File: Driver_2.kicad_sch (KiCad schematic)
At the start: 34 parts

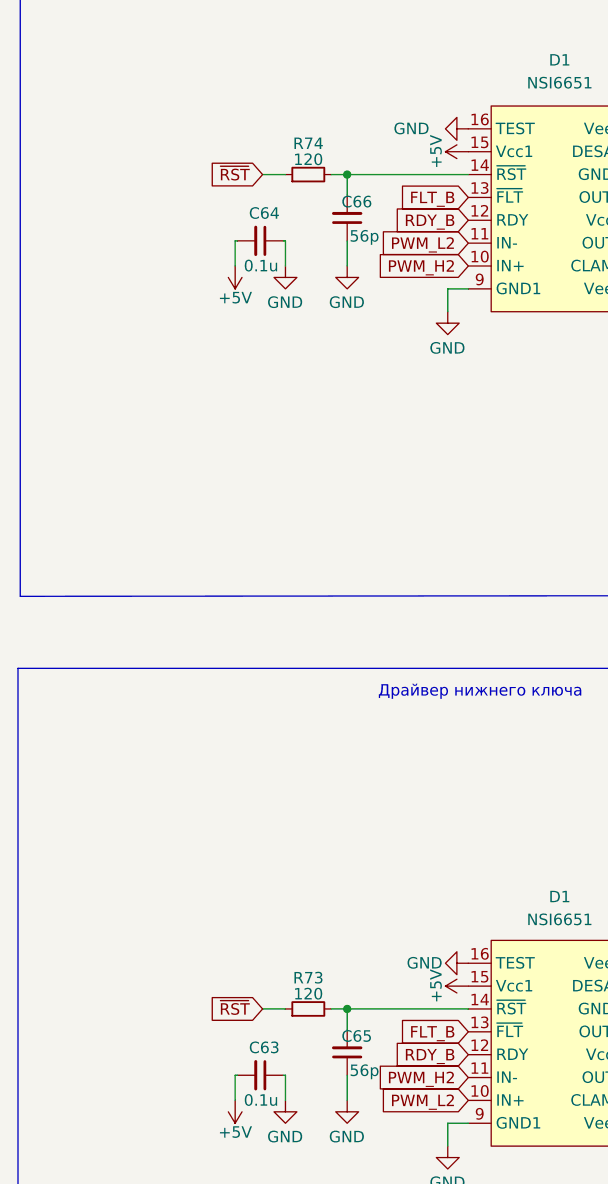
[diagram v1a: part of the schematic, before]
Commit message: Отправил на проверку в резонит: изменил BOM
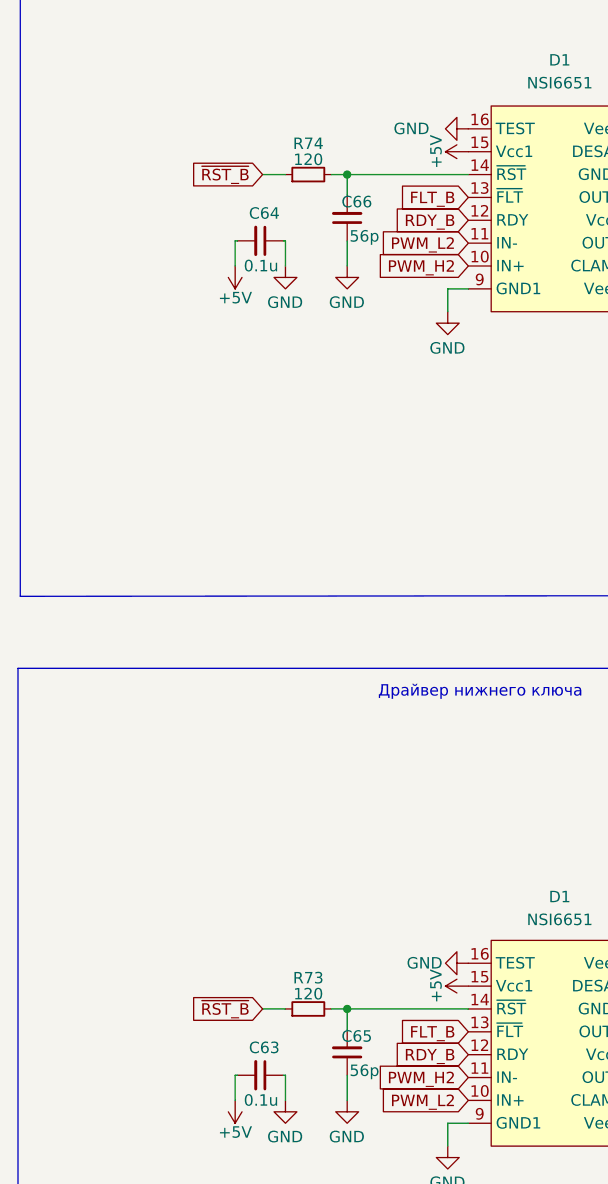
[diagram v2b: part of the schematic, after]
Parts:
- D41, D42, D60, D62: value MURS360T3G -> MURS160
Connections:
- net ~{RST} renamed ~{RST_B}
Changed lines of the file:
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@@
+		)
+	)
+	(global_label "~{RST_B}"
+		(shape input)
+		(at 58.42 146.05 180)
+		(fields_autoplaced yes)
+		(effects
+			(font
+				(size 1.27 1.27)
+			)
+			(justify right)
+		)
+		(property "Intersheetrefs" "${INTERSHEET_REFS}"
+			(at 49.7501 146.05 0)
+			(effects
+				(font
+					(size 1.27 1.27)
+				)
+				(justify right)
+				(hide yes)
+			)
 		)
 	)
@@
 		)
 	)
+	(global_label "~{RST_B}"
+		(shape input)
+		(at 58.42 53.34 180)
+		(fields_autoplaced yes)
+		(effects
+			(font
+				(size 1.27 1.27)
+			)
+			(justify right)
+		)
+		(property "Intersheetrefs" "${INTERSHEET_REFS}"
+			(at 49.7501 53.34 0)
+			(effects
+				(font
+					(size 1.27 1.27)
+				)
+				(justify right)
+				(hide yes)
+			)
+		)
+	)
 	(global_label "+15V_L2"
 		(shape input)
@@
 		)
 	)
-	(global_label "~{RST}"
-		(shape input)
-		(at 58.42 146.05 180)
-		(fields_autoplaced yes)
-		(effects
-			(font
-				(size 1.27 1.27)
-			)
-			(justify right)
-		)
-		(property "Intersheetrefs" "${INTERSHEET_REFS}"
-			(at 52.605 146.05 0)
-			(effects
-				(font
-					(size 1.27 1.27)
-				)
-				(justify right)
-				(hide yes)
-			)
-		)
-	)
 	(global_label "C3"
 		(shape input)
@@
 		)
 	)
-	(global_label "~{RST}"
-		(shape input)
-		(at 58.42 53.34 180)
-		(fields_autoplaced yes)
-		(effects
-			(font
-				(size 1.27 1.27)
-			)
-			(justify right)
-		)
-		(property "Intersheetrefs" "${INTERSHEET_REFS}"
-			(at 52.605 53.34 0)
-			(effects
-				(font
-					(size 1.27 1.27)
-				)
-				(justify right)
-				(hide yes)
-			)
-		)
-	)
 	(global_label "-15V_H2"
 		(shape input)
@@
 			)
 		)
-		(property "Value" "MURS360T3G"
+		(property "Value" "MURS160"
 			(at 131.318 68.834 0)
 			(effects
@@
 			)
 		)
-		(property "Value" "MURS360T3G"
+		(property "Value" "MURS160"
 			(at 153.924 146.05 0)
 			(effects
@@
 			)
 		)
-		(property "Value" "MURS360T3G"
+		(property "Value" "MURS160"
 			(at 131.318 73.914 0)
 			(effects
@@
 			)
 		)
-		(property "Value" "MURS360T3G"
+		(property "Value" "MURS160"
 			(at 148.844 146.05 0)
 			(effects

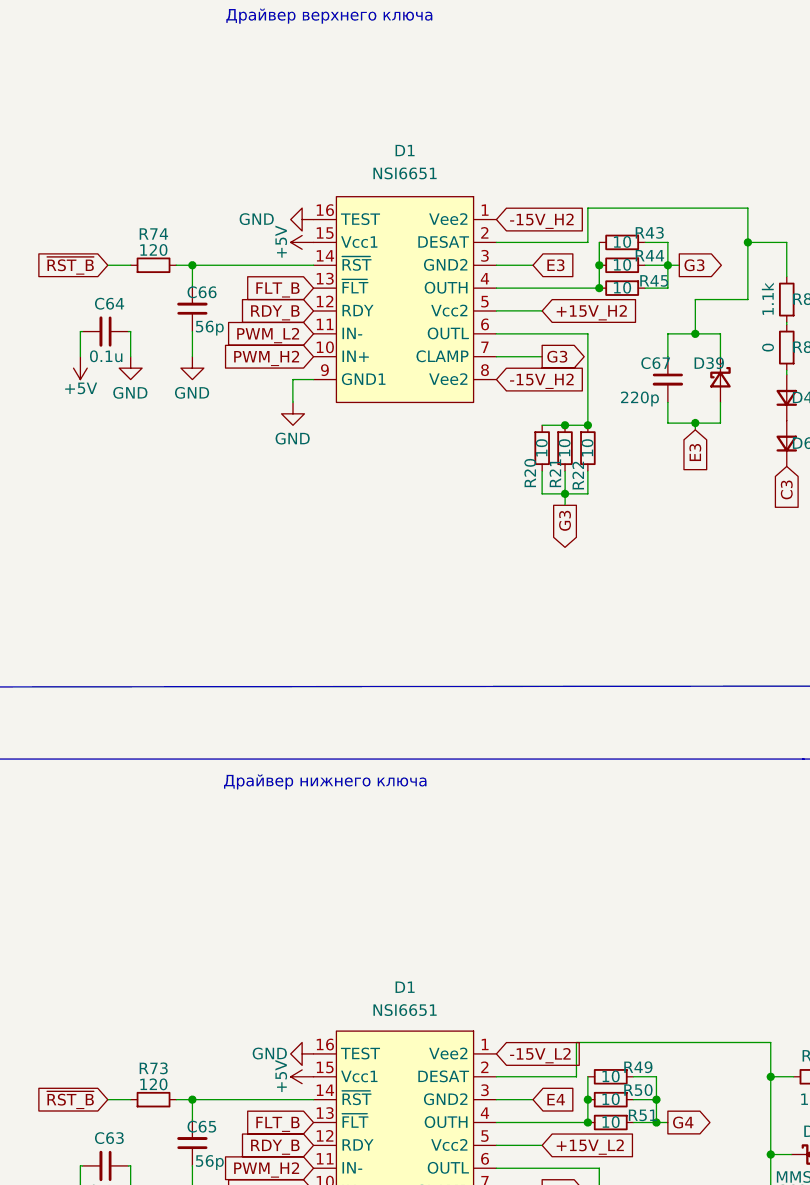
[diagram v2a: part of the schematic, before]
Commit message: Изменения: обновил BOM и названия в схеме
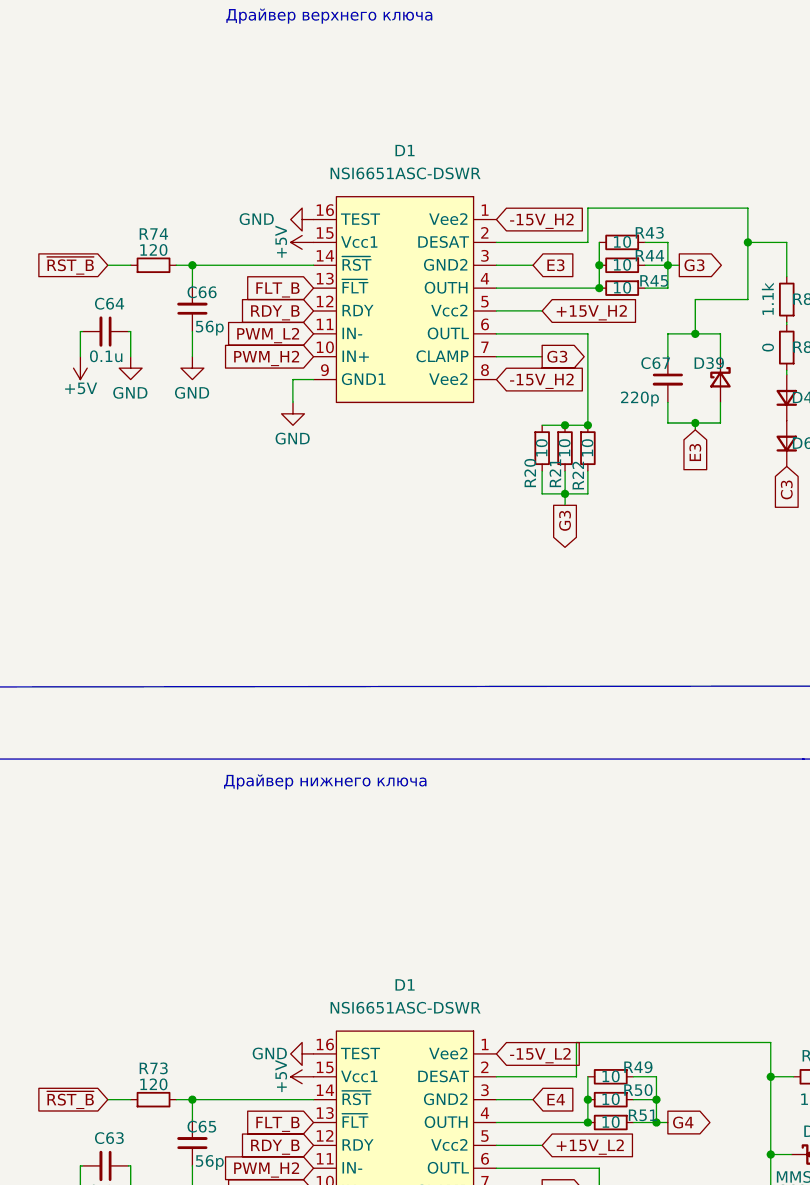
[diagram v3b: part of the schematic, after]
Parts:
- D1: value NSI6651 -> NSI6651ASC-DSWR
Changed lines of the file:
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@@
 			)
 		)
-		(property "Value" "NSI6651"
+		(property "Value" "NSI6651ASC-DSWR"
 			(at 91.44 43.18 0)
 			(effects
@@
 		(fields_autoplaced yes)
 		(property "Reference" "D1"
-			(at 91.44 133.604 0)
-			(effects
-				(font
-					(size 1.27 1.27)
-				)
-			)
-		)
-		(property "Value" "NSI6651"
-			(at 91.44 136.144 0)
-			(effects
-				(font
+			(at 91.44 133.35 0)
+			(effects
+				(font
+					(size 1.27 1.27)
+				)
+			)
+		)
+		(property "Value" "NSI6651ASC-DSWR"
+			(at 91.44 135.89 0)
+			(effects
+				(font

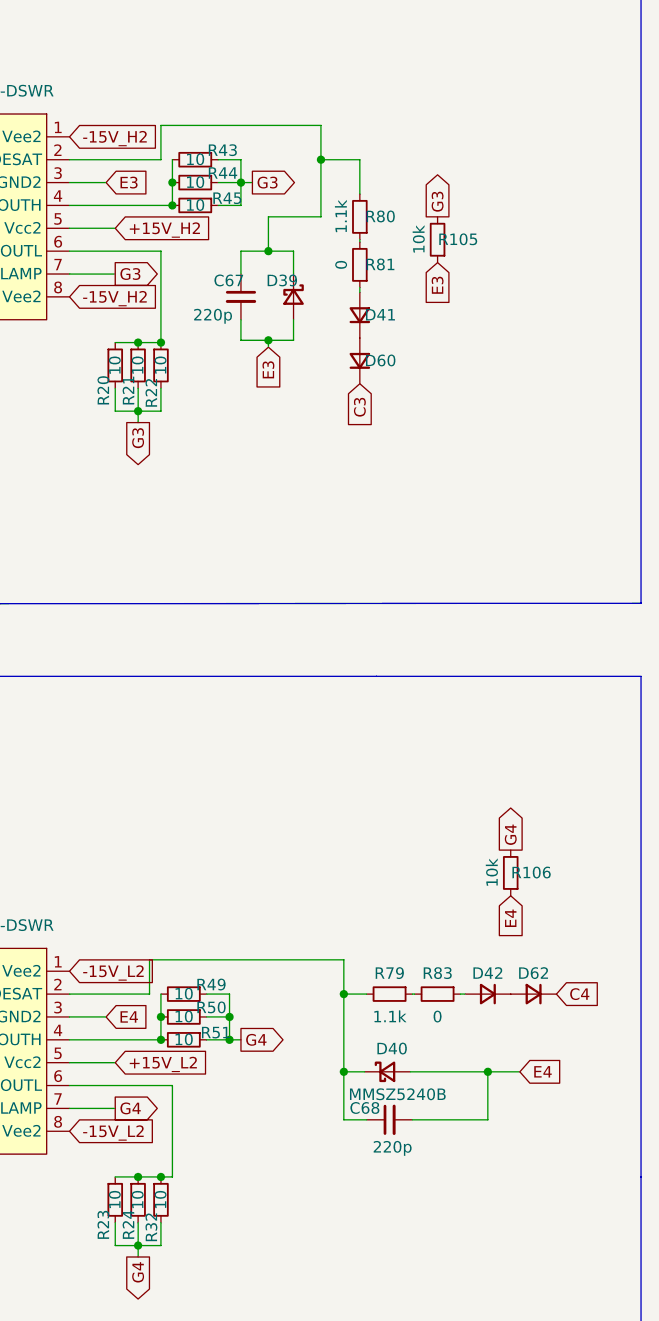
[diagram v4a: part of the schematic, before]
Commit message: Изменения: поменял трассировку полигонов, изменил трассировку цепи DESAT в фазе А
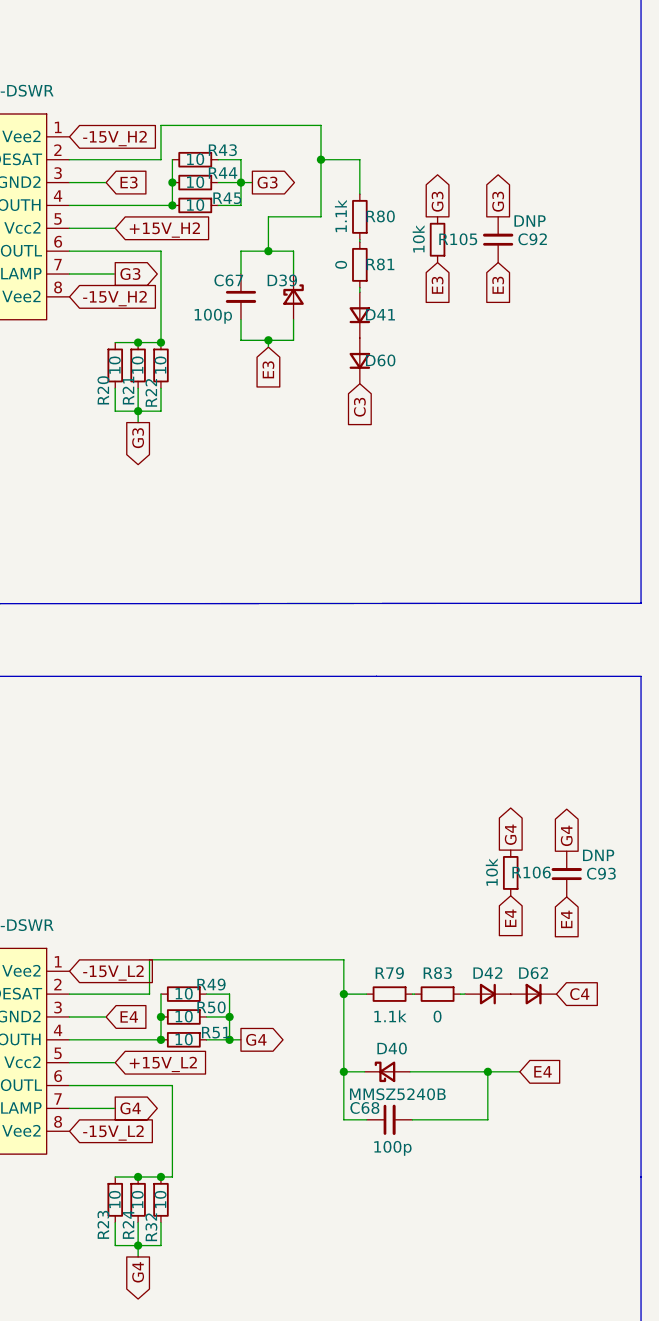
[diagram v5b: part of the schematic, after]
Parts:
- added C92, C93: DNP, Capacitor_SMD:C_0805_2012Metric_Pad1.18x1.45mm_HandSolder, symbol Device:C_Small
- C67, C68: value 220p -> 100p
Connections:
- net E3: now also C92.1
- net E4: now also C93.1
- net G3: now also C92.2
- net G4: now also C93.2
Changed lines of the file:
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@@
 		)
 	)
+	(global_label "E4"
+		(shape input)
+		(at 156.845 132.715 270)
+		(fields_autoplaced yes)
+		(effects
+			(font
+				(size 1.27 1.27)
+			)
+			(justify right)
+		)
+		(property "Intersheetrefs" "${INTERSHEET_REFS}"
+			(at 156.7656 137.4867 90)
+			(effects
+				(font
+					(size 1.27 1.27)
+				)
+				(justify right)
+				(hide yes)
+			)
+		)
+	)
 	(global_label "+15V_H2"
 		(shape input)
@@
 		)
 	)
+	(global_label "E3"
+		(shape input)
+		(at 149.225 62.23 270)
+		(fields_autoplaced yes)
+		(effects
+			(font
+				(size 1.27 1.27)
+			)
+			(justify right)
+		)
+		(property "Intersheetrefs" "${INTERSHEET_REFS}"
+			(at 149.1456 67.0017 90)
+			(effects
+				(font
+					(size 1.27 1.27)
+				)
+				(justify right)
+				(hide yes)
+			)
+		)
+	)
+	(global_label "G4"
+		(shape output)
+		(at 156.845 127.635 90)
+		(fields_autoplaced yes)
+		(effects
+			(font
+				(size 1.27 1.27)
+			)
+			(justify left)
+		)
+		(property "Intersheetrefs" "${INTERSHEET_REFS}"
+			(at 156.7656 122.7424 90)
+			(effects
+				(font
+					(size 1.27 1.27)
+				)
+				(justify left)
+				(hide yes)
+			)
+		)
+	)
 	(global_label "~{RST_B}"
 		(shape input)
@@
 	(global_label "G3"
 		(shape output)
+		(at 149.225 57.15 90)
+		(fields_autoplaced yes)
+		(effects
+			(font
+				(size 1.27 1.27)
+			)
+			(justify left)
+		)
+		(property "Intersheetrefs" "${INTERSHEET_REFS}"
+			(at 149.1456 52.2574 90)
+			(effects
+				(font
+					(size 1.27 1.27)
+				)
+				(justify left)
+				(hide yes)
+			)
+		)
+	)
+	(global_label "G3"
+		(shape output)
 		(at 109.22 80.01 270)
 		(fields_autoplaced yes)
@@
 	(symbol
 		(lib_id "Device:C_Small")
+		(at 156.845 130.175 180)
+		(unit 1)
+		(exclude_from_sim no)
+		(in_bom yes)
+		(on_board yes)
+		(dnp no)
+		(property "Reference" "C93"
+			(at 162.433 130.175 0)
+			(effects
+				(font
+					(size 1.27 1.27)
+				)
+				(justify left)
+			)
+		)
+		(property "Value" "DNP"
+			(at 162.179 128.143 0)
+			(effects
+				(font
+					(size 1.27 1.27)
+				)
+				(justify left)
+			)
+		)
+		(property "Footprint" "Capacitor_SMD:C_0805_2012Metric_Pad1.18x1.45mm_HandSolder"
+			(at 156.845 130.175 0)
+			(effects
+				(font
+					(size 1.27 1.27)
+				)
+				(hide yes)
+			)
+		)
+		(property "Datasheet" "~"
+			(at 156.845 130.175 0)
+			(effects
+				(font
+					(size 1.27 1.27)
+				)
+				(hide yes)
+			)
+		)
+		(property "Description" "Unpolarized capacitor, small symbol"
+			(at 156.845 130.175 0)
+			(effects
+				(font
+					(size 1.27 1.27)
+				)
+				(hide yes)
+			)
+		)
+		(pin "1"
+		)
+		(pin "2"
+		)
+		(instances
+			(project "Adapter"
+				(path "/e63e39d7-6ac0-4ffd-8aa3-1841a4541b55/7be86f5d-dd1f-4f1b-8cd0-4746349973df"
+					(reference "C93")
+					(unit 1)
+				)
+			)
+		)
+	)
+	(symbol
+		(lib_id "Device:C_Small")
 		(at 67.818 150.876 180)
 		(unit 1)
@@
 	)
 	(symbol
+		(lib_id "Device:C_Small")
+		(at 149.225 59.69 180)
+		(unit 1)
+		(exclude_from_sim no)
+		(in_bom yes)
+		(on_board yes)
+		(dnp no)
+		(property "Reference" "C92"
+			(at 154.813 59.69 0)
+			(effects
+				(font
+					(size 1.27 1.27)
+				)
+				(justify left)
+			)
+		)
+		(property "Value" "DNP"
+			(at 154.559 57.658 0)
+			(effects
+				(font
+					(size 1.27 1.27)
+				)
+				(justify left)
+			)
+		)
+		(property "Footprint" "Capacitor_SMD:C_0805_2012Metric_Pad1.18x1.45mm_HandSolder"
+			(at 149.225 59.69 0)
+			(effects
+				(font
+					(size 1.27 1.27)
+				)
+				(hide yes)
+			)
+		)
+		(property "Datasheet" "~"
+			(at 149.225 59.69 0)
+			(effects
+				(font
+					(size 1.27 1.27)
+				)
+				(hide yes)
+			)
+		)
+		(property "Description" "Unpolarized capacitor, small symbol"
+			(at 149.225 59.69 0)
+			(effects
+				(font
+					(size 1.27 1.27)
+				)
+				(hide yes)
+			)
+		)
+		(pin "1"
+		)
+		(pin "2"
+		)
+		(instances
+			(project "Adapter"
+				(path "/e63e39d7-6ac0-4ffd-8aa3-1841a4541b55/7be86f5d-dd1f-4f1b-8cd0-4746349973df"
+					(reference "C92")
+					(unit 1)
+				)
+			)
+		)
+	)
+	(symbol
 		(lib_id "Device:R_Small")
 		(at 111.76 73.66 0)
@@
 			)
 		)
-		(property "Value" "220p"
+		(property "Value" "100p"
 			(at 139.7 160.528 90)
 			(effects
@@
 			)
 		)
-		(property "Value" "220p"
+		(property "Value" "100p"
 			(at 115.316 68.072 0)
 			(effects

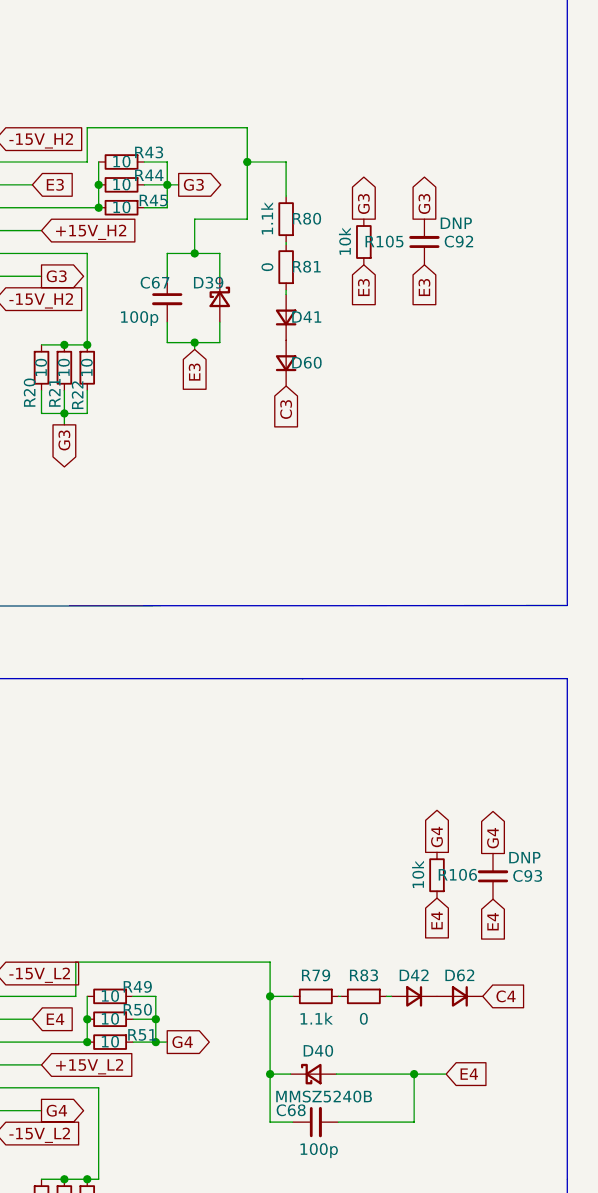
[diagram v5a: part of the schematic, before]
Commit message: VER2.1: переработал цепь DESAT
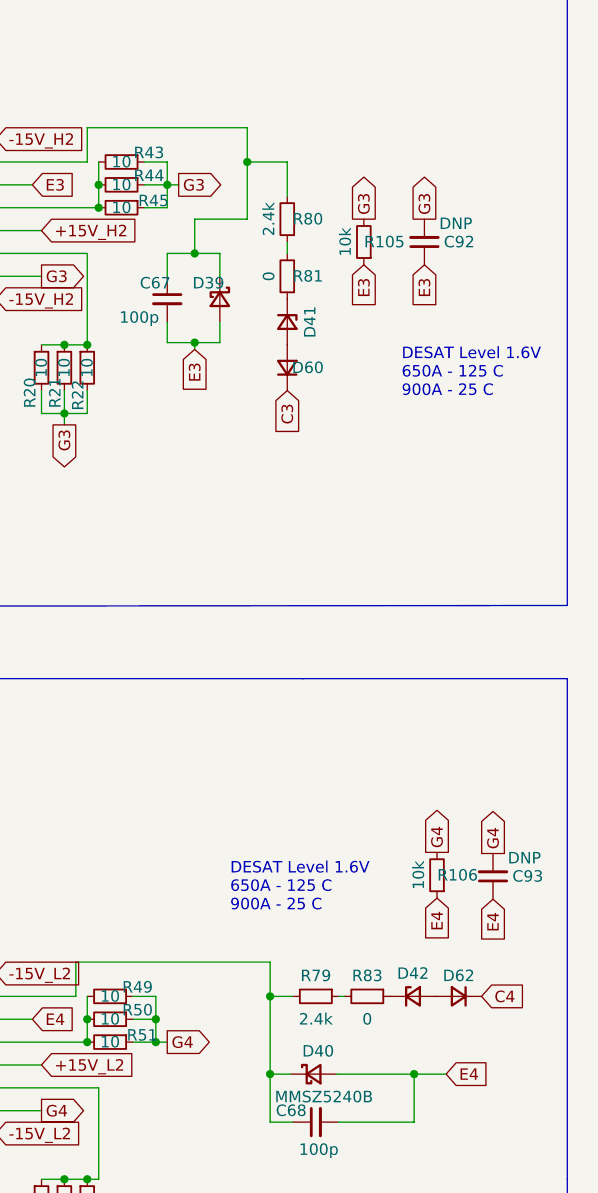
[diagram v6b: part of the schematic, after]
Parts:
- removed D41, D42: MURS160, Diode_SMD:D_SMA_Handsoldering, symbol Device:D_Small
- added D41, D42: MMSZ5232B, Diode_SMD:D_SOD-123, symbol Device:D_Zener_Small
- R79, R80: value 1.1k -> 2.4k
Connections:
- net at D60.2 (A): now also D41.2 (A)
- net at R81.1: now also D41.1 (K)
- net at D62.2 (A): now also D42.2 (A)
- net at R83.1: now also D42.1 (K)
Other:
- note added: "DESAT Level 1.6V 650A - 125 C 900A - 25 C"
- moved on the sheet: D60, R81
